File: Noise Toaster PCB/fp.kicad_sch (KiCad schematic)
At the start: 29 parts, among them J1 Line Out, SW1 Manual Gate, SW2 Repeat

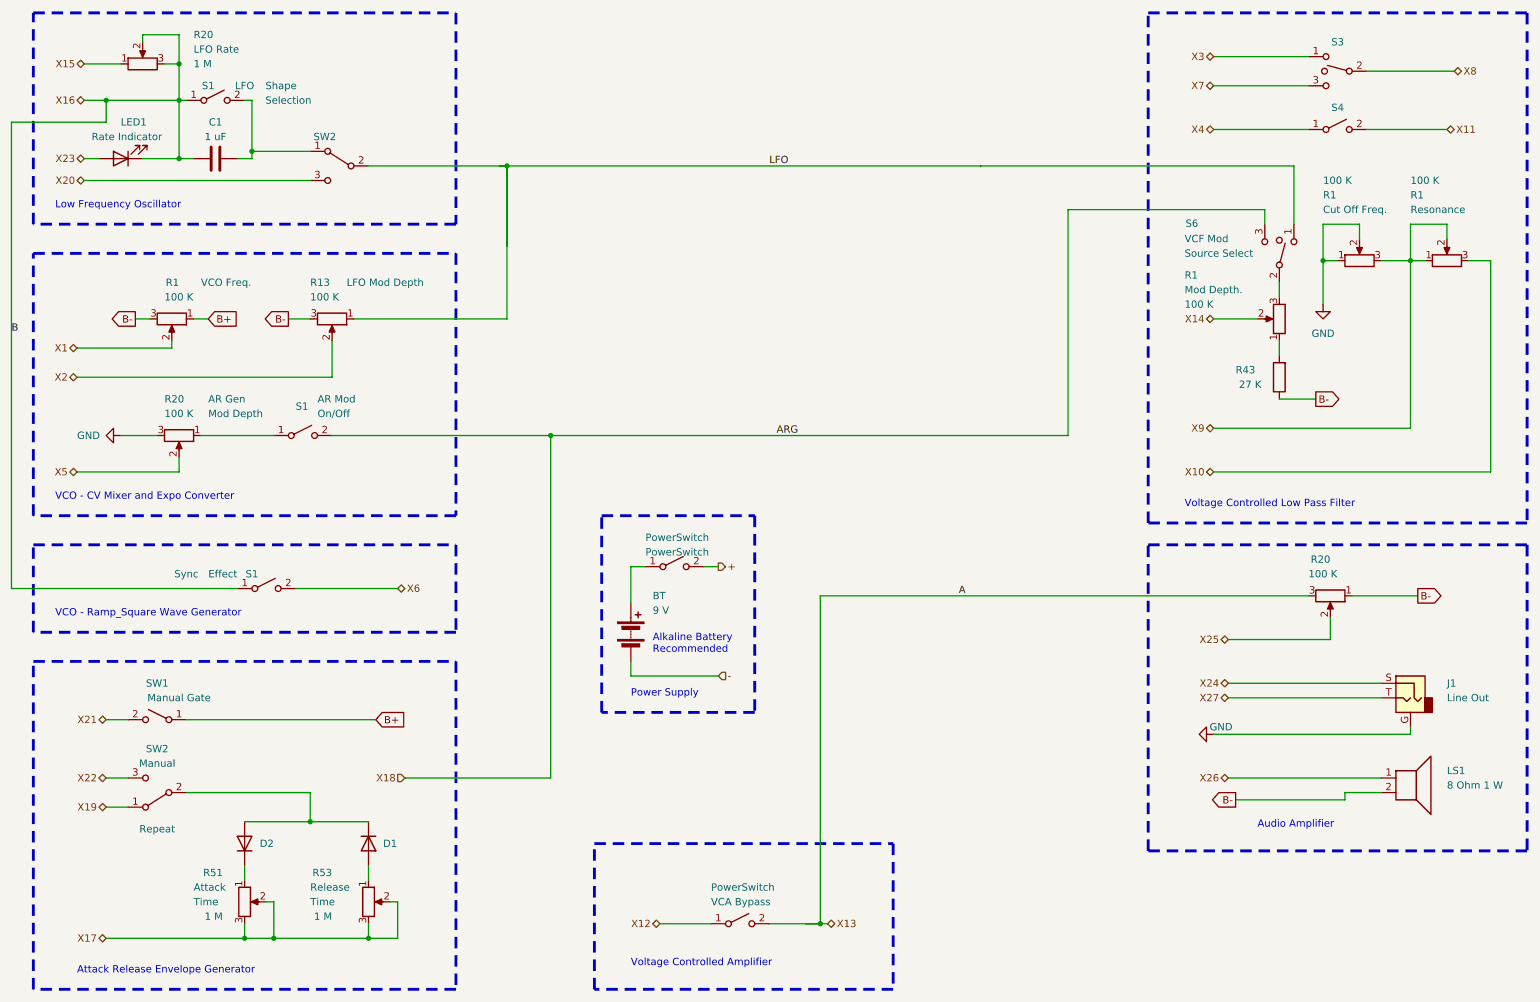
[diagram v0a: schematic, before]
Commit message: wireing and components have been checked
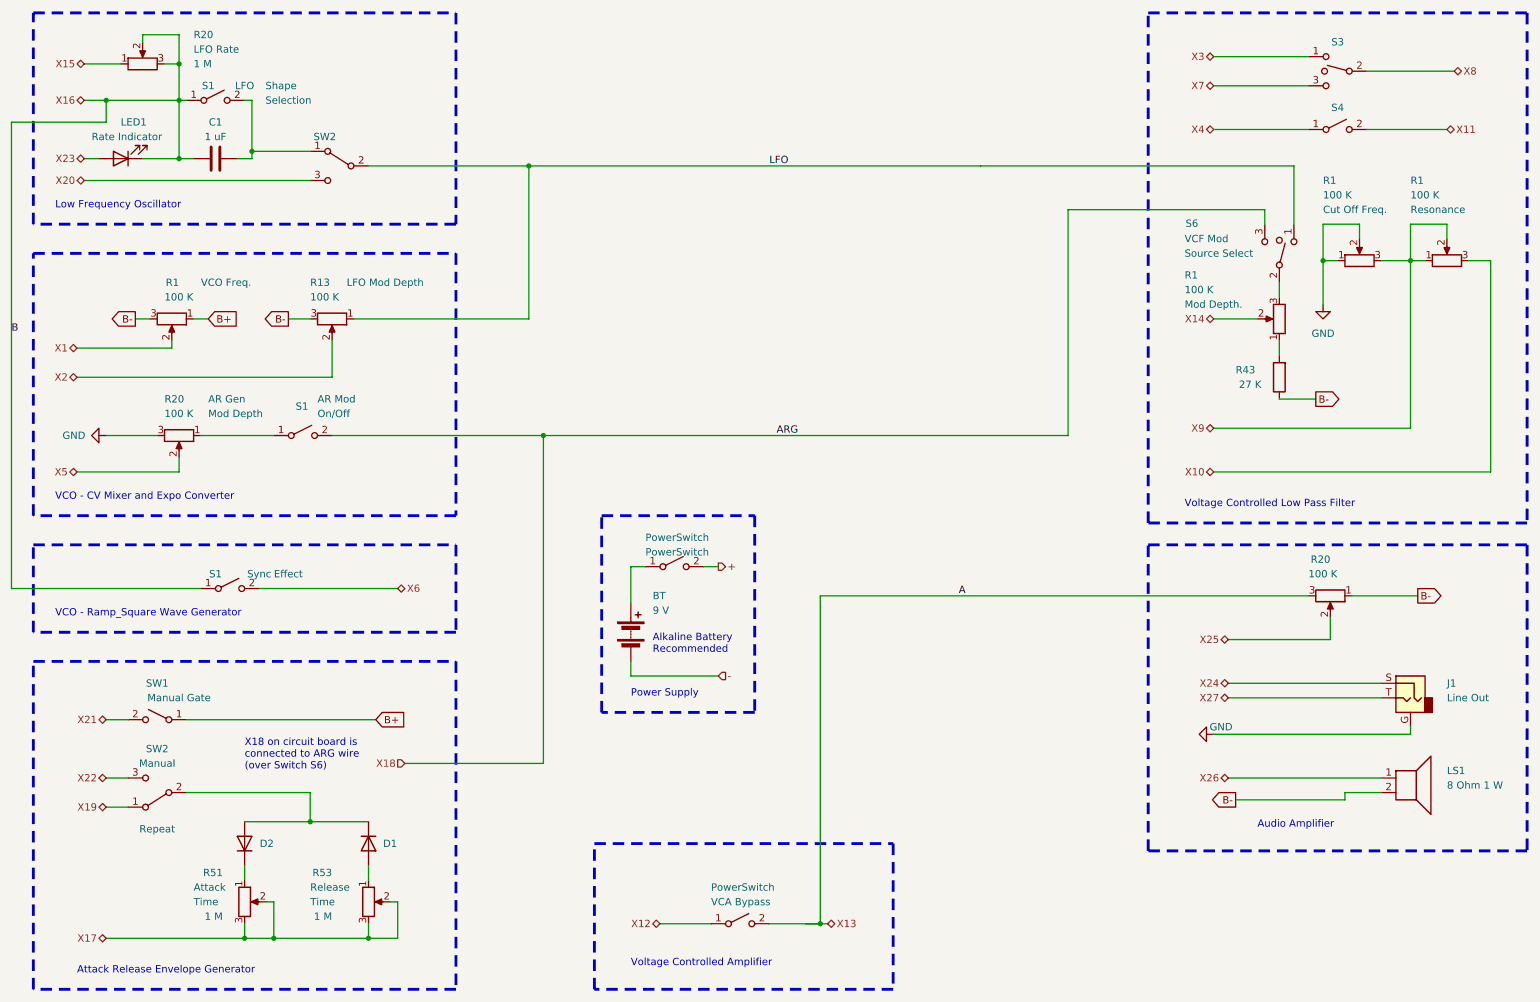
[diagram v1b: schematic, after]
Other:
- note added: "X18 on circuit board is connected to ARG wire (over Switch S6)"
- moved on the sheet: S1
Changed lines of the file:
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@@
   (junction (at 45.72 31.75) (diameter 0) (color 0 0 0 0)
   )
+  (junction (at 109.22 90.17) (diameter 0) (color 0 0 0 0)
+  )
   (junction (at 45.72 41.91) (diameter 0) (color 0 0 0 0)
   )
@@
   (junction (at 68.58 157.48) (diameter 0) (color 0 0 0 0)
   )
-  (junction (at 110.49 90.17) (diameter 0) (color 0 0 0 0)
-  )
   (junction (at 58.42 40.64) (diameter 0) (color 0 0 0 0)
   )
-  (junction (at 102.87 43.18) (diameter 0) (color 0 0 0 0)
-  )
   (junction (at 62.23 177.8) (diameter 0) (color 0 0 0 0)
   )
@@
   (junction (at 260.35 59.69) (diameter 0) (color 0 0 0 0)
   )
+  (junction (at 106.68 43.18) (diameter 0) (color 0 0 0 0)
+  )
   (wire (pts (xy 226.06 69.85) (xy 233.68 69.85))
     (stroke (width 0) (type default) (color 255 153 0 1))
   )
-  (wire (pts (xy 185.42 43.18) (xy 102.87 43.18))
-    (stroke (width 0) (type default) (color 255 153 0 1))
-  )
-  (wire (pts (xy 72.39 90.17) (xy 110.49 90.17))
-    (stroke (width 0) (type default) (color 255 157 0 1))
-  )
-  (wire (pts (xy 66.04 116.84) (xy 83.82 116.84))
+  (wire (pts (xy 185.42 43.18) (xy 106.68 43.18))
+    (stroke (width 0) (type default) (color 255 153 0 1))
+  )
+  (wire (pts (xy 72.39 90.17) (xy 109.22 90.17))
+    (stroke (width 0) (type default) (color 255 157 0 1))
+  )
+  (wire (pts (xy 59.69 116.84) (xy 83.82 116.84))
     (stroke (width 0) (type default) (color 255 153 0 1))
   )
@@
     (stroke (width 0) (type default) (color 255 153 0 1))
   )
-  (wire (pts (xy 76.2 69.85) (xy 102.87 69.85))
+  (wire (pts (xy 76.2 69.85) (xy 106.68 69.85))
     (stroke (width 0) (type default) (color 255 157 0 1))
   )
@@
     (stroke (width 0) (type default) (color 255 153 0 1))
   )
-  (wire (pts (xy 110.49 149.86) (xy 110.49 90.17))
+  (wire (pts (xy 109.22 147.32) (xy 109.22 90.17))
     (stroke (width 0) (type default) (color 255 157 0 1))
   )
@@
     (stroke (width 0) (type default))
   )
-  (wire (pts (xy 78.74 43.18) (xy 102.87 43.18))
-    (stroke (width 0) (type default) (color 255 157 0 1))
-  )
   (wire (pts (xy 226.06 96.52) (xy 274.32 96.52))
     (stroke (width 0) (type default) (color 255 153 0 1))
@@
     (stroke (width 0) (type default) (color 255 153 0 1))
   )
+  (wire (pts (xy 78.74 43.18) (xy 106.68 43.18))
+    (stroke (width 0) (type default) (color 255 157 0 1))
+  )
   (wire (pts (xy 68.58 69.85) (xy 64.77 69.85))
     (stroke (width 0) (type default) (color 255 153 0 1))
@@
     (stroke (width 0) (type default) (color 255 153 0 1))
   )
-  (wire (pts (xy 16.51 116.84) (xy 55.88 116.84))
+  (wire (pts (xy 16.51 116.84) (xy 49.53 116.84))
     (stroke (width 0) (type default) (color 255 157 0 1))
   )
@@
     (stroke (width 0) (type default) (color 255 153 0 1))
   )
-  (wire (pts (xy 35.56 90.17) (xy 41.91 90.17))
+  (wire (pts (xy 33.02 90.17) (xy 41.91 90.17))
     (stroke (width 0) (type default) (color 255 153 0 1))
   )
@@
     (stroke (width 0) (type default) (color 255 153 0 1))
   )
-  (wire (pts (xy 85.09 149.86) (xy 110.49 149.86))
+  (wire (pts (xy 85.09 147.32) (xy 109.22 147.32))
     (stroke (width 0) (type default) (color 255 157 0 1))
   )
@@
     (stroke (width 0) (type default) (color 255 153 0 1))
   )
-  (wire (pts (xy 102.87 43.18) (xy 102.87 69.85))
+  (wire (pts (xy 106.68 43.18) (xy 106.68 69.85))
     (stroke (width 0) (type default) (color 255 157 0 1))
   )
@@
     (stroke (width 0) (type default) (color 255 153 0 1))
   )
-  (wire (pts (xy 102.87 43.18) (xy 102.87 57.15))
-    (stroke (width 0) (type default) (color 255 153 0 1))
-  )
   (wire (pts (xy 33.02 154.94) (xy 36.83 154.94))
     (stroke (width 0) (type default) (color 255 153 0 1))
+  )
+  (wire (pts (xy 109.22 90.17) (xy 110.49 90.17))
+    (stroke (width 0) (type default) (color 255 157 0 1))
   )
   (wire (pts (xy 57.15 175.26) (xy 57.15 177.8))
@@
   )
   (wire (pts (xy 39.37 20.32) (xy 45.72 20.32))
-    (stroke (width 0) (type default) (color 255 153 0 1))
-  )
-  (wire (pts (xy 101.6 43.18) (xy 102.87 43.18))
     (stroke (width 0) (type default) (color 255 153 0 1))
   )
@@
   )
   (text "Power Supply" (at 124.46 135.89 0)
+    (effects (font (size 1.27 1.27)) (justify left bottom))
+  )
+  (text "X18 on circuit board is\nconnected to ARG wire \n(over Switch S6)"
+    (at 57.15 148.59 0)
     (effects (font (size 1.27 1.27)) (justify left bottom))
   )
@@
     (effects (font (size 1.27 1.27)) (justify right))
   )
-  (hierarchical_label "X18" (shape input) (at 85.09 149.86 180) (fields_autoplaced)
+  (hierarchical_label "X18" (shape input) (at 85.09 147.32 180) (fields_autoplaced)
     (effects (font (size 1.27 1.27)) (justify right))
   )
@@
     )
   )
-  (symbol (lib_id "power:GND") (at 35.56 90.17 270) (unit 1)
+  (symbol (lib_id "power:GND") (at 33.02 90.17 270) (unit 1)
     (in_bom yes) (on_board yes) (dnp no)
-    (property "Reference" "#PWR03" (at 29.21 90.17 0)
-      (effects (font (size 1.27 1.27)) hide)
-    )
-    (property "Value" "GND" (at 27.94 90.17 90)
-      (effects (font (size 1.27 1.27)) (justify left))
-    )
-    (property "Footprint" "" (at 35.56 90.17 0)
-      (effects (font (size 1.27 1.27)) hide)
-    )
-    (property "Datasheet" "" (at 35.56 90.17 0)
+    (property "Reference" "#PWR03" (at 26.67 90.17 0)
+      (effects (font (size 1.27 1.27)) hide)
+    )
+    (property "Value" "GND" (at 25.4 90.17 90)
+      (effects (font (size 1.27 1.27)) (justify left))
+    )
+    (property "Footprint" "" (at 33.02 90.17 0)
+      (effects (font (size 1.27 1.27)) hide)
+    )
+    (property "Datasheet" "" (at 33.02 90.17 0)
       (effects (font (size 1.27 1.27)) hide)
     )
@@
     )
   )
-  (symbol (lib_id "Switch:SW_SPST") (at 60.96 116.84 0) (unit 1)
-    (in_bom yes) (on_board no) (dnp no)
-    (property "Reference" "S1" (at 58.42 114.3 0)
-      (effects (font (size 1.27 1.27)))
-    )
-    (property "Value" "Sync" (at 46.99 114.3 0)
-      (effects (font (size 1.27 1.27)))
-    )
-    (property "Footprint" "" (at 60.96 116.84 0)
-      (effects (font (size 1.27 1.27)) hide)
-    )
-    (property "Datasheet" "~" (at 60.96 116.84 0)
-      (effects (font (size 1.27 1.27)) hide)
-    )
-    (property "Wert2" " Effect" (at 53.34 114.3 0)
+  (symbol (lib_id "Switch:SW_SPST") (at 54.61 116.84 0) (unit 1)
+    (in_bom yes) (on_board no) (dnp no)
+    (property "Reference" "S1" (at 52.07 114.3 0)
+      (effects (font (size 1.27 1.27)))
+    )
+    (property "Value" "Sync" (at 59.69 114.3 0)
+      (effects (font (size 1.27 1.27)))
+    )
+    (property "Footprint" "" (at 54.61 116.84 0)
+      (effects (font (size 1.27 1.27)) hide)
+    )
+    (property "Datasheet" "~" (at 54.61 116.84 0)
+      (effects (font (size 1.27 1.27)) hide)
+    )
+    (property "Wert2" " Effect" (at 64.77 114.3 0)
       (effects (font (size 1.27 1.27)))
     )
@@
       (effects (font (size 1.27 1.27)) (justify right))
     )
-    (property "Value" "100 K" (at 220.98 67.31 0)
+    (property "Value" "100 K" (at 220.98 64.77 0)
       (effects (font (size 1.27 1.27)) (justify right))
     )
@@
       (effects (font (size 1.27 1.27)) hide)
     )
-    (property "Beschreibung" "Mod Depth." (at 220.98 64.77 0)
+    (property "Beschreibung" "Mod Depth." (at 220.98 67.31 0)
       (effects (font (size 1.27 1.27)) (justify right))
     )
@@
   (symbol (lib_id "Device:R_Potentiometer") (at 251.46 59.69 90) (unit 1)
     (in_bom yes) (on_board no) (dnp no)
-    (property "Reference" "R1" (at 245.11 48.26 90)
-      (effects (font (size 1.27 1.27)) (justify right))
-    )
-    (property "Value" "100 K" (at 245.11 45.72 90)
+    (property "Reference" "R1" (at 245.11 45.72 90)
+      (effects (font (size 1.27 1.27)) (justify right))
+    )
+    (property "Value" "100 K" (at 245.11 48.26 90)
       (effects (font (size 1.27 1.27)) (justify right))
     )
@@
   (symbol (lib_id "Device:R_Potentiometer") (at 266.7 59.69 90) (unit 1)
     (in_bom yes) (on_board no) (dnp no)
-    (property "Reference" "R1" (at 260.35 48.26 90)
-      (effects (font (size 1.27 1.27)) (justify right))
-    )
-    (property "Value" "100 K" (at 260.35 45.72 90)
-      (effects (font (size 1.27 1.27)) (justify right))
-    )
+    (property "Reference" "R1" (at 260.35 45.72 90)
+      (effects (font (size 1.27 1.27)) (justify right))
+    )
+    (property "Value" "100 K" (at 260.35 48.26 90)
+      (effects (font (size 1.27 1.27)) (justify right))
+    )

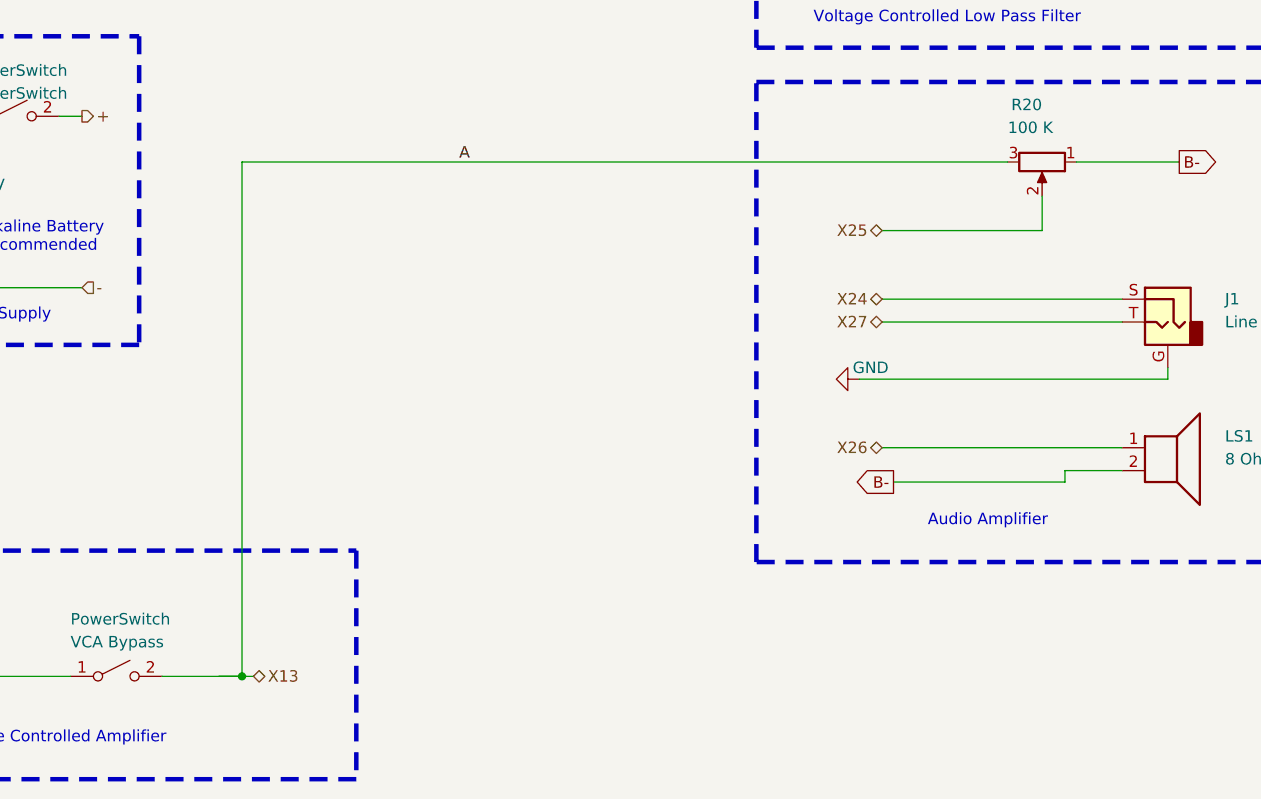
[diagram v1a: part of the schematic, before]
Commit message: applied footprints
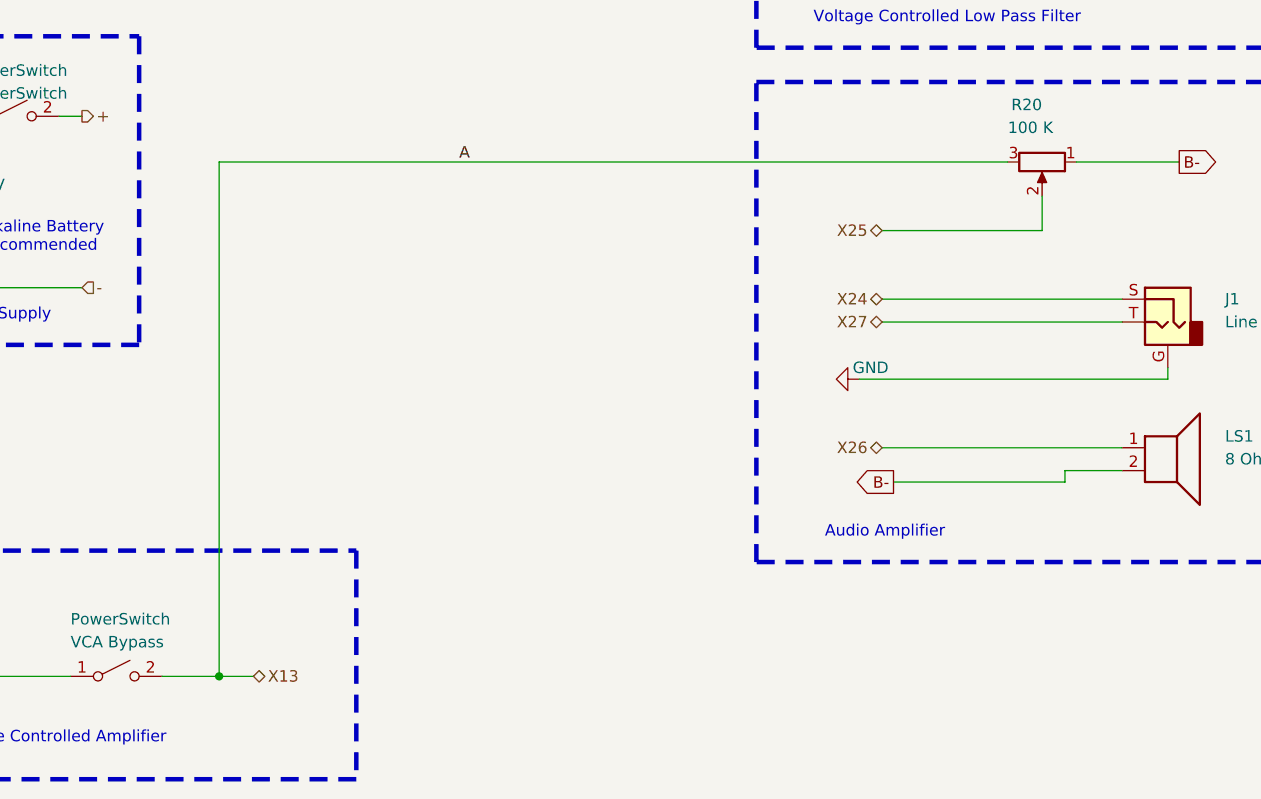
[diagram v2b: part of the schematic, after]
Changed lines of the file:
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@@
   (junction (at 45.72 41.91) (diameter 0) (color 0 0 0 0)
   )
-  (junction (at 157.48 175.26) (diameter 0) (color 0 0 0 0)
-  )
   (junction (at 33.02 31.75) (diameter 0) (color 0 0 0 0)
   )
@@
   )
   (junction (at 106.68 43.18) (diameter 0) (color 0 0 0 0)
+  )
+  (junction (at 154.94 175.26) (diameter 0) (color 0 0 0 0)
   )
   (wire (pts (xy 226.06 69.85) (xy 233.68 69.85))
@@
     (stroke (width 0) (type default) (color 255 153 0 1))
   )
-  (wire (pts (xy 157.48 118.11) (xy 242.57 118.11))
+  (wire (pts (xy 154.94 118.11) (xy 242.57 118.11))
     (stroke (width 0) (type default) (color 255 157 0 1))
   )
@@
     (stroke (width 0) (type default) (color 255 153 0 1))
   )
-  (wire (pts (xy 157.48 175.26) (xy 158.75 175.26))
-    (stroke (width 0) (type default) (color 255 153 0 1))
-  )
   (wire (pts (xy 248.92 152.4) (xy 255.27 152.4))
     (stroke (width 0) (type default) (color 255 153 0 1))
@@
     (stroke (width 0) (type default) (color 255 157 0 1))
   )
-  (wire (pts (xy 157.48 118.11) (xy 157.48 175.26))
-    (stroke (width 0) (type default) (color 255 157 0 1))
-  )
   (wire (pts (xy 58.42 31.75) (xy 58.42 40.64))
     (stroke (width 0) (type default) (color 255 153 0 1))
@@
     (stroke (width 0) (type default) (color 255 153 0 1))
   )
-  (wire (pts (xy 148.59 175.26) (xy 157.48 175.26))
+  (wire (pts (xy 148.59 175.26) (xy 154.94 175.26))
     (stroke (width 0) (type default) (color 255 153 0 1))
   )
@@
     (stroke (width 0) (type default) (color 255 157 0 1))
   )
+  (wire (pts (xy 154.94 175.26) (xy 158.75 175.26))
+    (stroke (width 0) (type default) (color 255 157 0 1))
+  )
   (wire (pts (xy 57.15 175.26) (xy 57.15 177.8))
     (stroke (width 0) (type default) (color 255 153 0 1))
@@
     (stroke (width 0) (type default) (color 255 153 0 1))
   )
+  (wire (pts (xy 154.94 118.11) (xy 154.94 175.26))
+    (stroke (width 0) (type default) (color 255 157 0 1))
+  )
   (wire (pts (xy 255.27 59.69) (xy 260.35 59.69))
     (stroke (width 0) (type default) (color 255 153 0 1))
@@
     (stroke (width 0) (type default) (color 255 153 0 1))
   )
-  (wire (pts (xy 157.48 175.26) (xy 154.94 175.26))
-    (stroke (width 0) (type default) (color 255 157 0 1))
-  )
   (wire (pts (xy 124.46 132.08) (xy 124.46 129.54))
     (stroke (width 0) (type default) (color 255 153 0 1))
@@
     (fill (type none))
   )
-  (text "Audio Amplifier" (at 233.68 158.75 0)
+  (text "Audio Amplifier" (at 222.25 160.02 0)
     (effects (font (size 1.27 1.27)) (justify left bottom))
   )

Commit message: placed pards of the pcb properly
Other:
- company: http://musicfromouterspace.com/analogsynth_new/NOISETOASTER/NOISETOASTER.php -> Music From Outer Space LLC
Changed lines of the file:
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@@
     (title "Front Panel")
     (rev "0.5")
-    (company "http://musicfromouterspace.com/analogsynth_new/NOISETOASTER/NOISETOASTER.php")
+    (company "Music From Outer Space LLC")
     (comment 1 "Licence: CC-BY-NC-SA")
     (comment 2 "Original Design by Ray Wilson")
-    (comment 3 "Music From Outer Space LLC")
+    (comment 3 "http://musicfromouterspace.com/analogsynth_new/NOISETOASTER/NOISETOASTER.php")
   )
   (junction (at 45.72 25.4) (diameter 0) (color 0 0 0 0)
